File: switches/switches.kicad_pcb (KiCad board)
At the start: 2 copper layers, 44 parts, among them J1 switchesOut, J10 Conn_01x01_Female, J11 Conn_01x01_Female, J12 Conn_01x01_Female, J2 Conn_01x01_Female, J3 Conn_01x01_Female, J4 Conn_01x01_Female, J5 Conn_01x01_Female, J6 Conn_01x01_Female, J7 Conn_01x01_Female, J8 Conn_01x01_Female, J9 Conn_01x01_Female, Q1 2N7002, Q2 2N7002, Q3 2N7002, Q4 2N7002, Q5 2N7002, Q6 2N7002

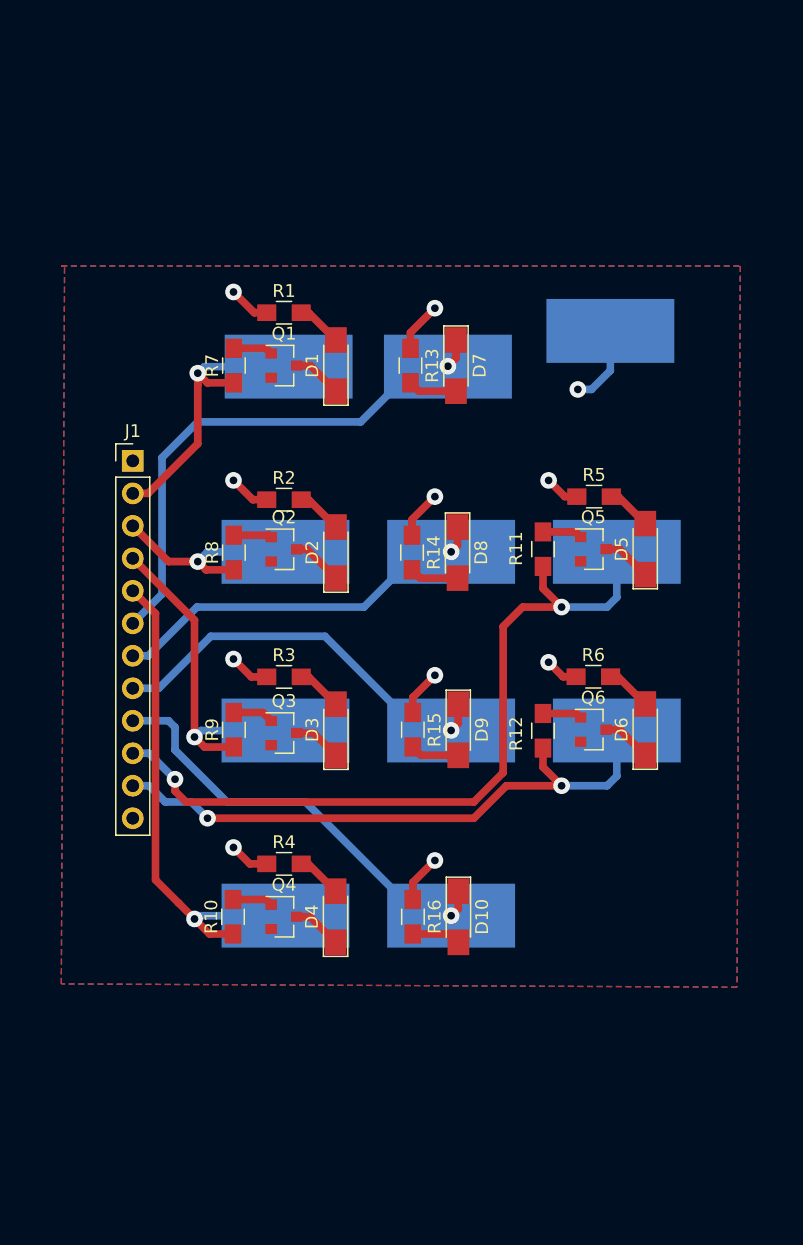
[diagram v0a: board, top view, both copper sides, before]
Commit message: designed and added proper cutlines for switches
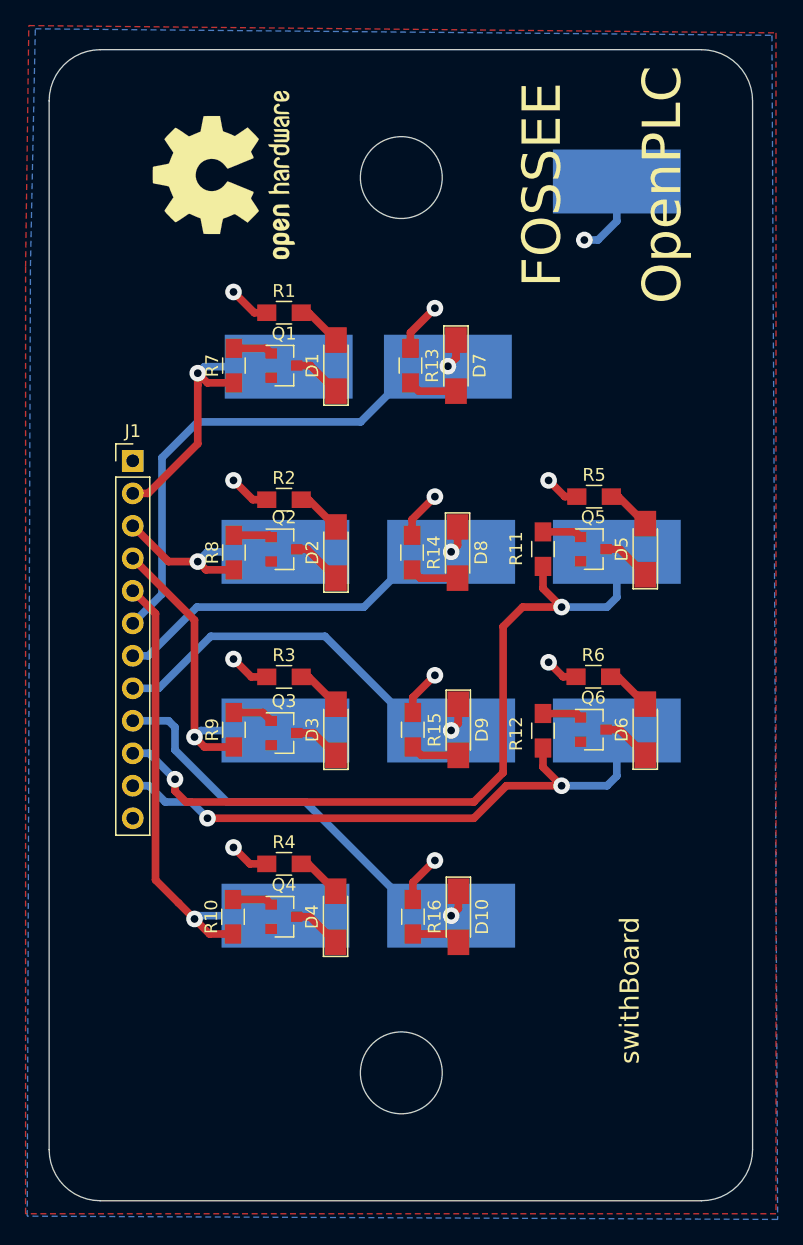
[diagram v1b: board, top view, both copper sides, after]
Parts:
- added REF***: OSHW-Logo2_14.6x12mm_SilkScreen, Symbols:OSHW-Logo2_14.6x12mm_SilkScreen, F.Cu at (104.9, 61.2)
- moved J2 11.7 mm to (135.6, 61.7)
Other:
- board outline added: 55 x 90 mm
- board text added: "FOSSEE"
- board text added: "OpenPLC"
- board text added: "swithBoard"

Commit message: changed switch PCB size to 9x5 cm
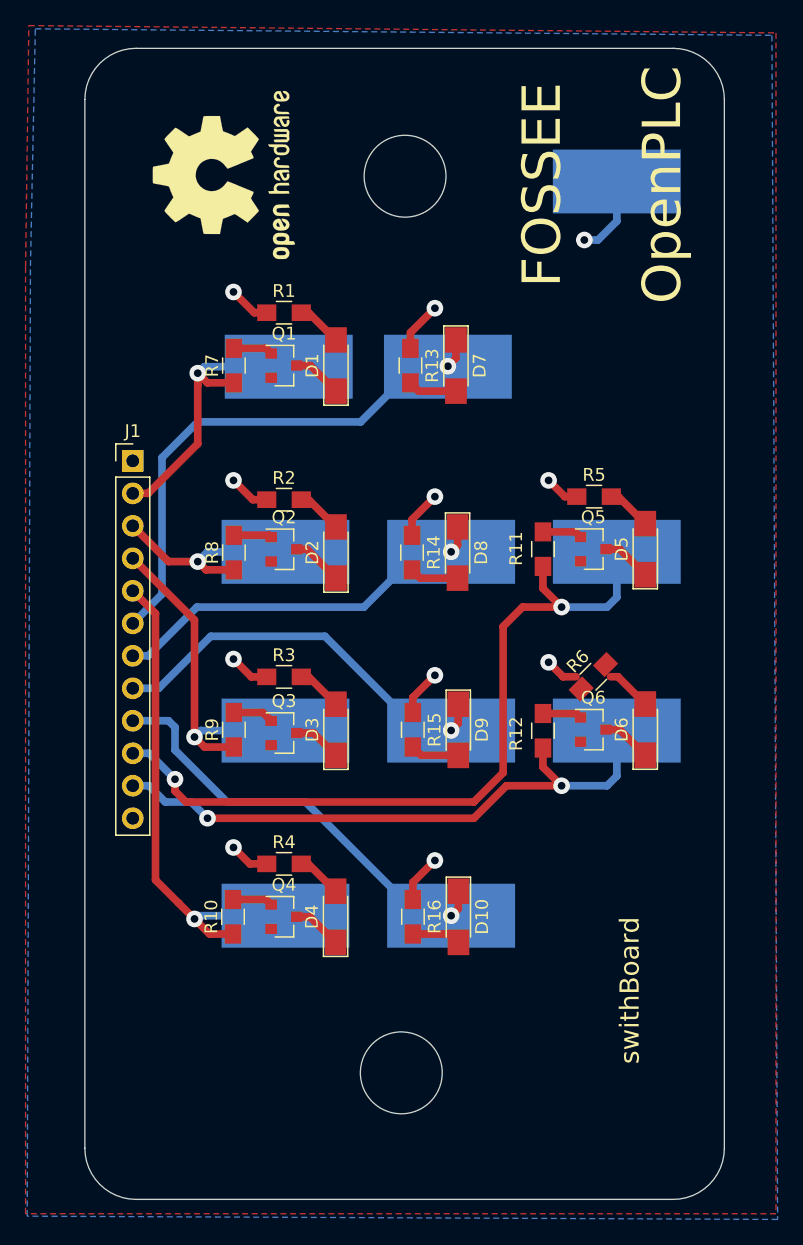
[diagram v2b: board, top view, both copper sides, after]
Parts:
- turned R6 to 45 degrees
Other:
- board size 55 x 90 mm -> 50 x 90 mm
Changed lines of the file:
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@@
   )
   (module Resistors_SMD:R_0805_HandSoldering (layer F.Cu)
-    (at 133.8 100.44345)
+    (at 133.8 100.44345 45)
     (descr "Resistor SMD 0805, hand soldering")
     (tags "resistor 0805")
     (attr smd)
-    (fp_text reference R6 (at 0 -1.7) (layer F.SilkS)
-      (effects (font (size 1 1) (thickness 0.15)))
-    )
-    (fp_text value R_US (at 0 1.75) (layer F.Fab)
-      (effects (font (size 1 1) (thickness 0.15)))
-    )
-    (fp_text user %R (at 0 0) (layer F.Fab)
+    (fp_text reference R6 (at 0 -1.7 45) (layer F.SilkS)
+      (effects (font (size 1 1) (thickness 0.15)))
+    )
+    (fp_text value R_US (at 0 1.75 45) (layer F.Fab)
+      (effects (font (size 1 1) (thickness 0.15)))
+    )
+    (fp_text user %R (at 0 0 45) (layer F.Fab)
       (effects (font (size 0.5 0.5) (thickness 0.075)))
     )
@@
     (fp_line (start 2.35 0.9) (end 2.35 -0.9) (layer F.CrtYd) (width 0.05))
     (fp_line (start 2.35 0.9) (end -2.35 0.9) (layer F.CrtYd) (width 0.05))
-    (pad 1 smd rect (at -1.35 0) (size 1.5 1.3) (layers F.Cu F.Paste F.Mask)
+    (pad 1 smd rect (at -1.35 0 45) (size 1.5 1.3) (layers F.Cu F.Paste F.Mask)
       (net 19 +5V))
-    (pad 2 smd rect (at 1.35 0) (size 1.5 1.3) (layers F.Cu F.Paste F.Mask)
+    (pad 2 smd rect (at 1.35 0 45) (size 1.5 1.3) (layers F.Cu F.Paste F.Mask)
       (net 24 "Net-(D6-Pad2)"))
     (model ${KISYS3DMOD}/Resistors_SMD.3dshapes/R_0805.wrl
@@
       (xy -0.026262 -5.547126) (xy 0 -5.547126) (xy 0.209014 -5.547002)) (layer F.SilkS) (width 0.01))
   )
-  (dimension 55.118 (width 0.3) (layer Margin)
-    (gr_text "55.118 mm" (at 118.745 36.762) (layer Margin)
+  (dimension 89.916 (width 0.3) (layer F.Mask)
+    (gr_text "89.916 mm" (at 163.898 96.266 270) (layer F.Mask)
       (effects (font (size 1.5 1.5) (thickness 0.3)))
     )
-    (feature1 (pts (xy 146.304 54.864) (xy 146.304 38.275579)))
-    (feature2 (pts (xy 91.186 54.864) (xy 91.186 38.275579)))
-    (crossbar (pts (xy 91.186 38.862) (xy 146.304 38.862)))
-    (arrow1a (pts (xy 146.304 38.862) (xy 145.177496 39.448421)))
-    (arrow1b (pts (xy 146.304 38.862) (xy 145.177496 38.275579)))
-    (arrow2a (pts (xy 91.186 38.862) (xy 92.312504 39.448421)))
-    (arrow2b (pts (xy 91.186 38.862) (xy 92.312504 38.275579)))
-  )
-  (dimension 89.916 (width 0.3) (layer Margin)
-    (gr_text "89.916 mm" (at 179.646 96.52 270) (layer Margin)
+    (feature1 (pts (xy 139.954 141.224) (xy 162.384421 141.224)))
+    (feature2 (pts (xy 139.954 51.308) (xy 162.384421 51.308)))
+    (crossbar (pts (xy 161.798 51.308) (xy 161.798 141.224)))
+    (arrow1a (pts (xy 161.798 141.224) (xy 161.211579 140.097496)))
+    (arrow1b (pts (xy 161.798 141.224) (xy 162.384421 140.097496)))
+    (arrow2a (pts (xy 161.798 51.308) (xy 161.211579 52.434504)))
+    (arrow2b (pts (xy 161.798 51.308) (xy 162.384421 52.434504)))
+  )
+  (dimension 50.038 (width 0.3) (layer F.Mask)
+    (gr_text "50.038 mm" (at 118.999 41.334) (layer F.Mask)
       (effects (font (size 1.5 1.5) (thickness 0.3)))
     )
-    (feature1 (pts (xy 142.494 141.478) (xy 178.132421 141.478)))
-    (feature2 (pts (xy 142.494 51.562) (xy 178.132421 51.562)))
-    (crossbar (pts (xy 177.546 51.562) (xy 177.546 141.478)))
-    (arrow1a (pts (xy 177.546 141.478) (xy 176.959579 140.351496)))
-    (arrow1b (pts (xy 177.546 141.478) (xy 178.132421 140.351496)))
-    (arrow2a (pts (xy 177.546 51.562) (xy 176.959579 52.688504)))
-    (arrow2b (pts (xy 177.546 51.562) (xy 178.132421 52.688504)))
-  )
+    (feature1 (pts (xy 144.018 55.88) (xy 144.018 42.847579)))
+    (feature2 (pts (xy 93.98 55.88) (xy 93.98 42.847579)))
+    (crossbar (pts (xy 93.98 43.434) (xy 144.018 43.434)))
+    (arrow1a (pts (xy 144.018 43.434) (xy 142.891496 44.020421)))
+    (arrow1b (pts (xy 144.018 43.434) (xy 142.891496 42.847579)))
+    (arrow2a (pts (xy 93.98 43.434) (xy 95.106504 44.020421)))
+    (arrow2b (pts (xy 93.98 43.434) (xy 95.106504 42.847579)))
+  )
+  (gr_line (start 98.044 51.308) (end 140.044 51.308) (layer Edge.Cuts) (width 0.1))
+  (gr_arc (start 140.044 137.308) (end 140.044 141.308) (angle -90) (layer Edge.Cuts) (width 0.1))
+  (gr_circle (center 119.079327 61.308) (end 119.079326 58.108) (layer Edge.Cuts) (width 0.1))
+  (gr_line (start 140.044 141.308) (end 98.044 141.308) (layer Edge.Cuts) (width 0.1))
+  (gr_arc (start 98.044 137.308) (end 94.044 137.308) (angle -90) (layer Edge.Cuts) (width 0.1))
+  (gr_line (start 144.044 55.308) (end 144.044 137.308) (layer Edge.Cuts) (width 0.1))
+  (gr_line (start 94.044 137.308) (end 94.044 55.308) (layer Edge.Cuts) (width 0.1))
+  (gr_arc (start 98.044 55.308) (end 98.044 51.308) (angle -90) (layer Edge.Cuts) (width 0.1))
+  (gr_arc (start 140.044 55.308) (end 144.044 55.308) (angle -90) (layer Edge.Cuts) (width 0.1))
   (gr_text swithBoard (at 136.652 124.968 90) (layer F.SilkS)
     (effects (font (size 1.5 1.5) (thickness 0.3)))
@@
   )
   (gr_circle (center 118.785327 131.414) (end 118.785327 128.214) (layer Edge.Cuts) (width 0.1))
-  (gr_circle (center 118.785327 61.414) (end 118.785327 58.214) (layer Edge.Cuts) (width 0.1))
-  (gr_line (start 146.25 137.414) (end 146.25 55.414) (layer Edge.Cuts) (width 0.1))
-  (gr_arc (start 142.25 55.414) (end 146.25 55.414) (angle -90) (layer Edge.Cuts) (width 0.1))
-  (gr_line (start 95.25 51.414) (end 142.25 51.414) (layer Edge.Cuts) (width 0.1))
-  (gr_line (start 142.25 141.414) (end 95.25 141.414) (layer Edge.Cuts) (width 0.1))
-  (gr_arc (start 142.25 137.414) (end 142.25 141.414) (angle -90) (layer Edge.Cuts) (width 0.1))
-  (gr_arc (start 95.25 55.414) (end 95.25 51.414) (angle -90) (layer Edge.Cuts) (width 0.1))
-  (gr_line (start 91.25 137.414) (end 91.25 55.414) (layer Edge.Cuts) (width 0.1))
-  (gr_arc (start 95.25 137.414) (end 91.25 137.414) (angle -90) (layer Edge.Cuts) (width 0.1))
   (via (at 131.318 108.966) (size 1.3) (drill 0.6) (layers F.Cu B.Cu) (net 1))
   (segment (start 129.862 106.018) (end 129.862 107.51) (width 0.6) (layer F.Cu) (net 1))

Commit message: corrected the mounting-scre-hole sizes to 3mm dia. drew symmetrical cutline for motor. updated README with new board images.
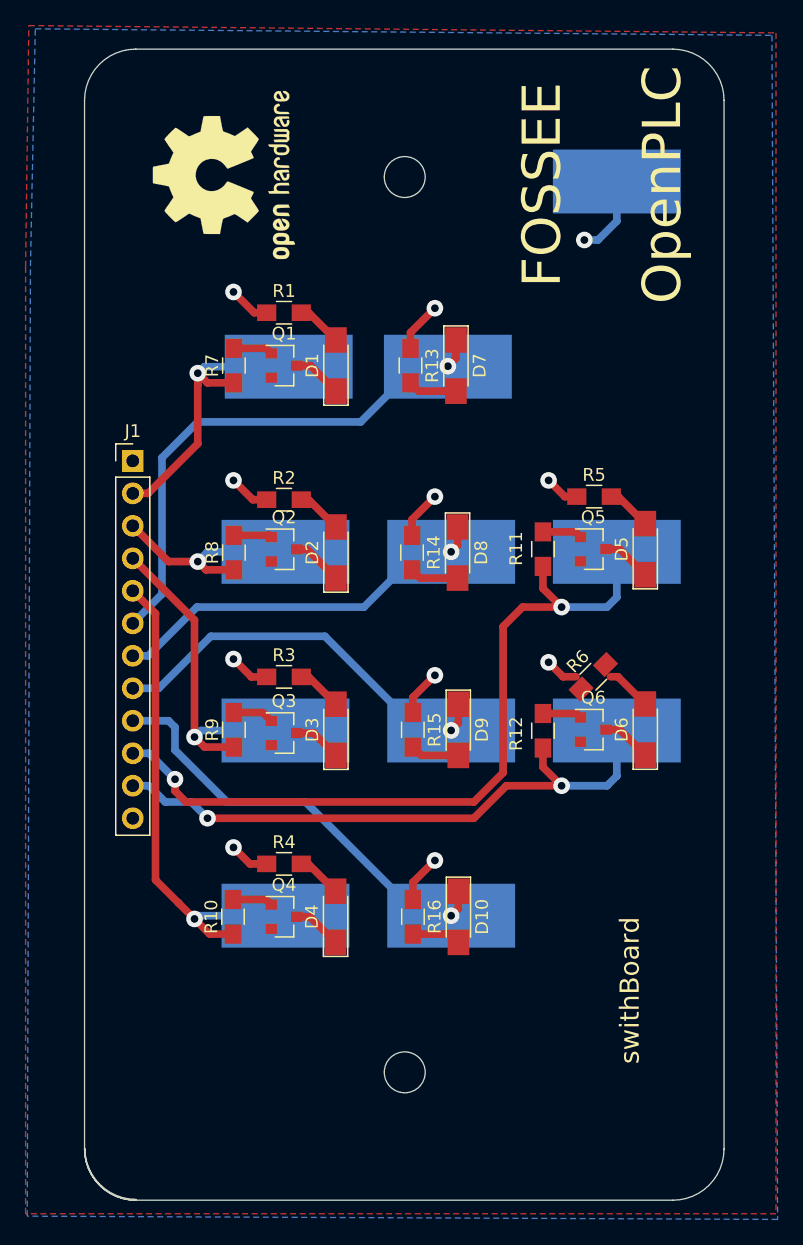
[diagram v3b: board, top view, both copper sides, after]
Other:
- outline, holes or cut-outs redrawn
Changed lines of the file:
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@@
   (general
     (thickness 1.6)
-    (drawings 15)
+    (drawings 17)
     (tracks 175)
     (zones 0)
@@
       (xy -0.026262 -5.547126) (xy 0 -5.547126) (xy 0.209014 -5.547002)) (layer F.SilkS) (width 0.01))
   )
-  (dimension 89.916 (width 0.3) (layer F.Mask)
-    (gr_text "89.916 mm" (at 163.898 96.266 270) (layer F.Mask)
+  (dimension 50.0001 (width 0.3) (layer Margin)
+    (gr_text "50.000 mm" (at 118.973596 42.647849 0.1145914062) (layer Margin)
       (effects (font (size 1.5 1.5) (thickness 0.3)))
     )
-    (feature1 (pts (xy 139.954 141.224) (xy 162.384421 141.224)))
-    (feature2 (pts (xy 139.954 51.308) (xy 162.384421 51.308)))
-    (crossbar (pts (xy 161.798 51.308) (xy 161.798 141.224)))
-    (arrow1a (pts (xy 161.798 141.224) (xy 161.211579 140.097496)))
-    (arrow1b (pts (xy 161.798 141.224) (xy 162.384421 140.097496)))
-    (arrow2a (pts (xy 161.798 51.308) (xy 161.211579 52.434504)))
-    (arrow2b (pts (xy 161.798 51.308) (xy 162.384421 52.434504)))
-  )
-  (dimension 50.038 (width 0.3) (layer F.Mask)
-    (gr_text "50.038 mm" (at 118.999 41.334) (layer F.Mask)
+    (feature1 (pts (xy 144 55.8) (xy 143.976623 44.111426)))
+    (feature2 (pts (xy 94 55.9) (xy 93.976623 44.211426)))
+    (crossbar (pts (xy 93.977796 44.797845) (xy 143.977796 44.697845)))
+    (arrow1a (pts (xy 143.977796 44.697845) (xy 142.852467 45.286518)))
+    (arrow1b (pts (xy 143.977796 44.697845) (xy 142.850122 44.113678)))
+    (arrow2a (pts (xy 93.977796 44.797845) (xy 95.10547 45.382012)))
+    (arrow2b (pts (xy 93.977796 44.797845) (xy 95.103125 44.209172)))
+  )
+  (dimension 90.000056 (width 0.3) (layer Margin)
+    (gr_text "90.000 mm" (at 154.701205 96.38361 270.063662) (layer Margin)
       (effects (font (size 1.5 1.5) (thickness 0.3)))
     )
-    (feature1 (pts (xy 144.018 55.88) (xy 144.018 42.847579)))
-    (feature2 (pts (xy 93.98 55.88) (xy 93.98 42.847579)))
-    (crossbar (pts (xy 93.98 43.434) (xy 144.018 43.434)))
-    (arrow1a (pts (xy 144.018 43.434) (xy 142.891496 44.020421)))
-    (arrow1b (pts (xy 144.018 43.434) (xy 142.891496 42.847579)))
-    (arrow2a (pts (xy 93.98 43.434) (xy 95.106504 44.020421)))
-    (arrow2b (pts (xy 93.98 43.434) (xy 95.106504 42.847579)))
-  )
-  (gr_line (start 98.044 51.308) (end 140.044 51.308) (layer Edge.Cuts) (width 0.1))
-  (gr_arc (start 140.044 137.308) (end 140.044 141.308) (angle -90) (layer Edge.Cuts) (width 0.1))
-  (gr_circle (center 119.079327 61.308) (end 119.079326 58.108) (layer Edge.Cuts) (width 0.1))
-  (gr_line (start 140.044 141.308) (end 98.044 141.308) (layer Edge.Cuts) (width 0.1))
+    (feature1 (pts (xy 140 141.4) (xy 153.237627 141.385292)))
+    (feature2 (pts (xy 139.9 51.4) (xy 153.137627 51.385292)))
+    (crossbar (pts (xy 152.551206 51.385943) (xy 152.651206 141.385943)))
+    (arrow1a (pts (xy 152.651206 141.385943) (xy 152.063534 140.260092)))
+    (arrow1b (pts (xy 152.651206 141.385943) (xy 153.236375 140.258788)))
+    (arrow2a (pts (xy 152.551206 51.385943) (xy 151.966037 52.513098)))
+    (arrow2b (pts (xy 152.551206 51.385943) (xy 153.138878 52.511794)))
+  )
+  (gr_circle (center 119.053327 131.372) (end 119.053327 129.772) (layer Edge.Cuts) (width 0.1))
   (gr_arc (start 98.044 137.308) (end 94.044 137.308) (angle -90) (layer Edge.Cuts) (width 0.1))
-  (gr_line (start 144.044 55.308) (end 144.044 137.308) (layer Edge.Cuts) (width 0.1))
-  (gr_line (start 94.044 137.308) (end 94.044 55.308) (layer Edge.Cuts) (width 0.1))
-  (gr_arc (start 98.044 55.308) (end 98.044 51.308) (angle -90) (layer Edge.Cuts) (width 0.1))
-  (gr_arc (start 140.044 55.308) (end 144.044 55.308) (angle -90) (layer Edge.Cuts) (width 0.1))
+  (gr_arc (start 98.018 137.372) (end 94.018 137.372) (angle -90) (layer Edge.Cuts) (width 0.1))
+  (gr_line (start 140.018 141.372) (end 98.018 141.372) (layer Edge.Cuts) (width 0.1))
+  (gr_line (start 140.018 51.372) (end 98.018 51.372) (layer Edge.Cuts) (width 0.1))
+  (gr_arc (start 140.018 55.372) (end 144.018 55.372) (angle -90) (layer Edge.Cuts) (width 0.1))
+  (gr_line (start 144.018 137.372) (end 144.018 55.372) (layer Edge.Cuts) (width 0.1))
+  (gr_arc (start 140.018 137.372) (end 140.018 141.372) (angle -90) (layer Edge.Cuts) (width 0.1))
+  (gr_arc (start 98.018 137.372) (end 94.018 137.372) (angle -90) (layer Edge.Cuts) (width 0.1))
+  (gr_line (start 94.018 55.372) (end 94.018 137.372) (layer Edge.Cuts) (width 0.1))
+  (gr_arc (start 98.018 55.372) (end 98.018 51.372) (angle -90) (layer Edge.Cuts) (width 0.1))
+  (gr_circle (center 119.053327 61.372) (end 119.053327 59.771999) (layer Edge.Cuts) (width 0.1))
   (gr_text swithBoard (at 136.652 124.968 90) (layer F.SilkS)
     (effects (font (size 1.5 1.5) (thickness 0.3)))
@@
     (effects (font (size 3 3) (thickness 0.5)))
   )
-  (gr_circle (center 118.785327 131.414) (end 118.785327 128.214) (layer Edge.Cuts) (width 0.1))
   (via (at 131.318 108.966) (size 1.3) (drill 0.6) (layers F.Cu B.Cu) (net 1))
   (segment (start 129.862 106.018) (end 129.862 107.51) (width 0.6) (layer F.Cu) (net 1))
